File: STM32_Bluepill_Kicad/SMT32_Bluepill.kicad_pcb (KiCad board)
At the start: 2 copper layers, 2 parts, among them IC1 RT9193-33GB, U1 STM32F103C8Tx

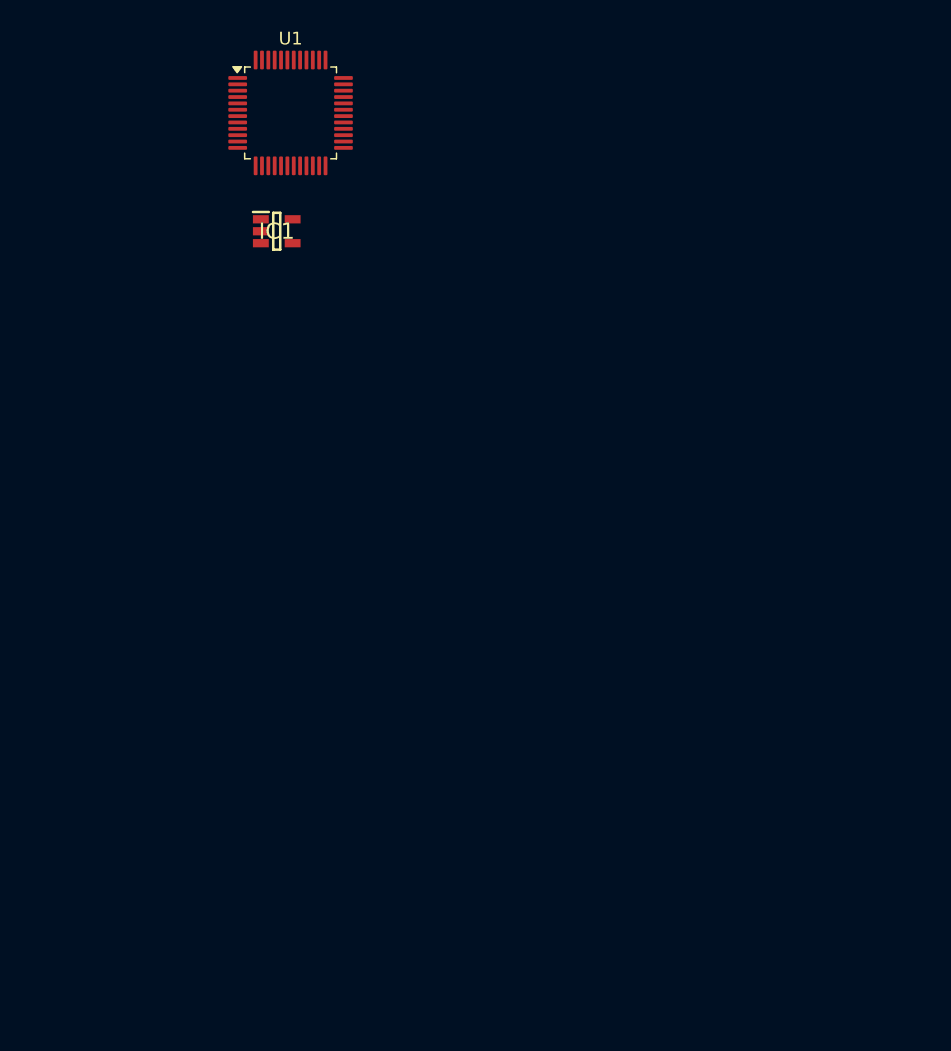
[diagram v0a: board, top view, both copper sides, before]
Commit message: Schematic done, PCB 50%
Component placements still undone
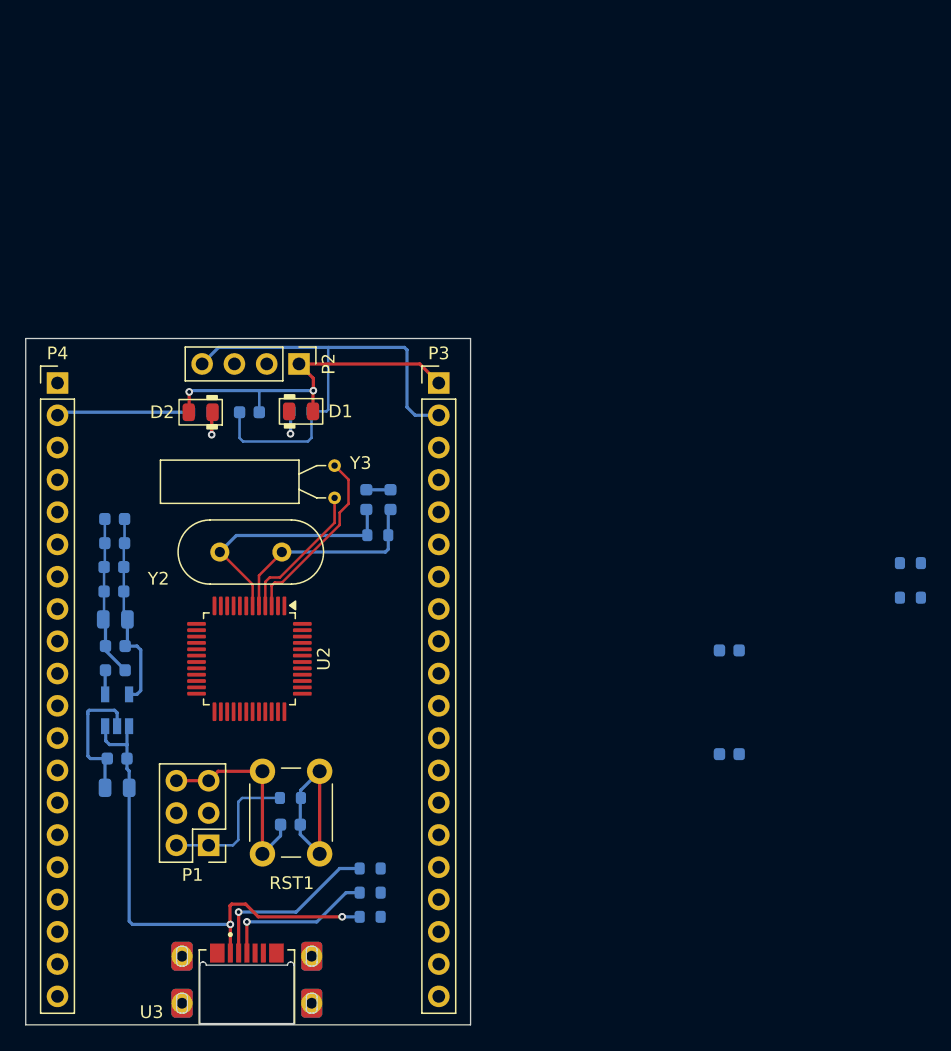
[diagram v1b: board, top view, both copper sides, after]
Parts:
- added C1: 104_0603, PCM_Capacitor_SMD_AKL:C_0603_1608Metric, B.Cu at (35.1, 52.3)
- added C10: 104_0603, PCM_Capacitor_SMD_AKL:C_0603_1608Metric, B.Cu at (24.4, 64.5)
- added C11: 104_0603, PCM_Capacitor_SMD_AKL:C_0603_1608Metric, B.Cu at (24.4, 66.4)
- added C12: 20pF_0603, PCM_Capacitor_SMD_AKL:C_0603_1608Metric, B.Cu at (72.9, 79.2)
- added C13: 20pF_0603, PCM_Capacitor_SMD_AKL:C_0603_1608Metric, B.Cu at (46.2, 59.2)
- added C14: 20pF_0603, PCM_Capacitor_SMD_AKL:C_0603_1608Metric, B.Cu at (44.3, 59.2)
- added C15: 223_0603, PCM_Capacitor_SMD_AKL:C_0603_1608Metric, B.Cu at (24.6, 72.6)
- added C2: 105_0603, PCM_Capacitor_SMD_AKL:C_0603_1608Metric, B.Cu at (38.3, 84.8)
- added C3: 104_0603, PCM_Capacitor_SMD_AKL:C_0603_1608Metric, B.Cu at (24.5, 60.7)
- added C4: 104_0603, PCM_Capacitor_SMD_AKL:C_0603_1608Metric, B.Cu at (24.5, 62.6)
- added C5: 105_0805, PCM_Capacitor_SMD_AKL:C_0805_2012Metric, B.Cu at (24.7, 81.8)
- added C6: 106_0805, PCM_Capacitor_SMD_AKL:C_0805_2012Metric, B.Cu at (24.6, 68.6)
- added C7: 104_0603, PCM_Capacitor_SMD_AKL:C_0603_1608Metric, B.Cu at (24.7, 79.5)
- added C8: 104_0603, PCM_Capacitor_SMD_AKL:C_0603_1608Metric, B.Cu at (24.6, 70.7)
- added C9: 20pF_0603, PCM_Capacitor_SMD_AKL:C_0603_1608Metric, B.Cu at (72.9, 71.0)
- added D1: LED_0805_Red, PCM_LED_SMD_AKL:LED_0805_2012Metric, F.Cu at (39.2, 52.2)
- added D2: LED_0805_Blue, PCM_LED_SMD_AKL:LED_0805_2012Metric, F.Cu at (31.3, 52.3)
- added P1: PINHD_2x3_Male, Connector_PinHeader_2.54mm:PinHeader_2x03_P2.54mm_Vertical, F.Cu at (31.9, 86.4)
- added P2: PINHD_1x4_Male, Connector_PinHeader_2.54mm:PinHeader_1x04_P2.54mm_Vertical, F.Cu at (39.0, 48.5)
- added P3: PINHD_1x20_Male, Connector_PinHeader_2.54mm:PinHeader_1x20_P2.54mm_Vertical, F.Cu at (50.0, 50.0)
- added P4: PINHD_1x20_Male, Connector_PinHeader_2.54mm:PinHeader_1x20_P2.54mm_Vertical, F.Cu at (20.0, 50.0)
- added R1: 510_0603, PCM_Resistor_SMD_AKL:R_0603_1608Metric, B.Cu at (39.2, 52.2)
- added R10: 4K7_0603, PCM_Resistor_SMD_AKL:R_0603_1608Metric, B.Cu at (44.6, 92.0)
- added R11: 20_0603, PCM_Resistor_SMD_AKL:R_0603_1608Metric, B.Cu at (44.6, 90.1)
- added R2: 10K_0603, PCM_Resistor_SMD_AKL:R_0603_1608Metric, B.Cu at (38.3, 82.7)
- added R3: 100K_0603, PCM_Resistor_SMD_AKL:R_0603_1608Metric, B.Cu at (87.1, 64.2)
- added R4: 100K_0603, PCM_Resistor_SMD_AKL:R_0603_1608Metric, B.Cu at (87.1, 66.9)
- added R5: 510_0603, PCM_Resistor_SMD_AKL:R_0603_1608Metric, B.Cu at (31.3, 52.3)
- added R6: 1M_0603, PCM_Resistor_SMD_AKL:R_0603_1608Metric, B.Cu at (45.2, 62.0)
- added R9: 20_0603, PCM_Resistor_SMD_AKL:R_0603_1608Metric, B.Cu at (44.6, 88.2)
- added RST1: Push_Button, Button_Switch_THT:SW_PUSH_6mm, F.Cu at (36.1, 87.0)
- added U3: 10103593-0001LF, USBmicro_10103593-0001LF:AMPHENOL_10103593-0001LF, F.Cu at (34.9, 98.8)
- added Y2: Crystal_8MHz, Crystal:Crystal_HC49-4H_Vertical, F.Cu at (37.6, 63.3)
- added Y3: Crystal_32.768kHz, Crystal:Crystal_AT310_D3.0mm_L10.0mm_Horizontal, F.Cu at (41.8, 56.5)
- U1: renamed from IC1; moved to B.Cu
- moved U2 43.1 mm to (35.1, 71.7), turned to -90 degrees
- moved U1 39.7 mm to (24.7, 75.8), turned to 90 degrees
- renumbered U1 to U2
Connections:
- U1 pad 1: unconnected-(IC1-VIN-Pad1) -> +5V
- U1 pad 2: unconnected-(IC1-GND-Pad2) -> GND
- U1 pad 3: unconnected-(IC1-EN-Pad3) -> +5V
- U1 pad 4: unconnected-(IC1-BP-Pad4) -> Net-(U1-BP)
- U1 pad 5: unconnected-(IC1-VOUT-Pad5) -> +3V3
- U2 pad 1: unconnected-(U1-VBAT-Pad1) -> VBAT
- U2 pad 10: unconnected-(U1-PA0-Pad10) -> PA0
- U2 pad 11: unconnected-(U1-PA1-Pad11) -> PA1
- U2 pad 12: unconnected-(U1-PA2-Pad12) -> PA2
- U2 pad 13: unconnected-(U1-PA3-Pad13) -> PA3
- U2 pad 14: unconnected-(U1-PA4-Pad14) -> PA4
- U2 pad 15: unconnected-(U1-PA5-Pad15) -> PA5
- U2 pad 16: unconnected-(U1-PA6-Pad16) -> PA6
- U2 pad 17: unconnected-(U1-PA7-Pad17) -> PA7
- U2 pad 18: unconnected-(U1-PB0-Pad18) -> PB0
- U2 pad 19: unconnected-(U1-PB1-Pad19) -> PB1
- U2 pad 2: unconnected-(U1-PC13-Pad2) -> PC13
- U2 pad 20: unconnected-(U1-PB2-Pad20) -> BOOT1
- U2 pad 21: unconnected-(U1-PB10-Pad21) -> PB10
- U2 pad 22: unconnected-(U1-PB11-Pad22) -> PB11
- U2 pad 23: Net-(U1-VSS-Pad23) -> GND
- U2 pad 24: unconnected-(U1-VDD-Pad24) -> +3V3
- U2 pad 25: unconnected-(U1-PB12-Pad25) -> PB12
- U2 pad 26: unconnected-(U1-PB13-Pad26) -> PB13
- U2 pad 27: unconnected-(U1-PB14-Pad27) -> PB14
- U2 pad 28: unconnected-(U1-PB15-Pad28) -> PB15
- U2 pad 29: unconnected-(U1-PA8-Pad29) -> PA8
- U2 pad 3: unconnected-(U1-PC14-Pad3) -> PC14
- U2 pad 30: unconnected-(U1-PA9-Pad30) -> PA9
- U2 pad 31: unconnected-(U1-PA10-Pad31) -> PA10
- U2 pad 32: unconnected-(U1-PA11-Pad32) -> PA11
- U2 pad 33: unconnected-(U1-PA12-Pad33) -> PA12
- U2 pad 34: unconnected-(U1-PA13-Pad34) -> SWDIO
- U2 pad 35: Net-(U1-VSS-Pad23) -> GND
- U2 pad 36: unconnected-(U1-VDD-Pad36) -> +3V3
- U2 pad 37: unconnected-(U1-PA14-Pad37) -> SWDCLK
- U2 pad 38: unconnected-(U1-PA15-Pad38) -> PA15
- U2 pad 39: unconnected-(U1-PB3-Pad39) -> PB3
- U2 pad 4: unconnected-(U1-PC15-Pad4) -> PC15
- U2 pad 40: unconnected-(U1-PB4-Pad40) -> PB4
- U2 pad 41: unconnected-(U1-PB5-Pad41) -> PB5
- U2 pad 42: unconnected-(U1-PB6-Pad42) -> PB6
- U2 pad 43: unconnected-(U1-PB7-Pad43) -> PB7
- U2 pad 44: unconnected-(U1-BOOT0-Pad44) -> BOOT0
- U2 pad 45: unconnected-(U1-PB8-Pad45) -> PB8
- U2 pad 46: unconnected-(U1-PB9-Pad46) -> PB9
- U2 pad 47: Net-(U1-VSS-Pad23) -> GND
- U2 pad 48: unconnected-(U1-VDD-Pad48) -> +3V3
- U2 pad 5: unconnected-(U1-PD0-Pad5) -> OSCIN
- U2 pad 6: unconnected-(U1-PD1-Pad6) -> OSCOUT
- U2 pad 7: unconnected-(U1-NRST-Pad7) -> NRST
- U2 pad 8: unconnected-(U1-VSSA-Pad8) -> GND
- U2 pad 9: unconnected-(U1-VDDA-Pad9) -> +3V3
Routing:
- net GND: track 0.00 -> 81.5 mm
- net +3V3: track 0.00 -> 56.5 mm, vias 0 -> 2
- net +5V: track 0.00 -> 40.9 mm, vias 0 -> 2
- net OSCOUT: track 0.00 -> 19.5 mm
- net OSCIN: track 0.00 -> 17.1 mm
- net PC14: track 0.00 -> 14.3 mm
- net Net-(C2-Pad1): track 0.00 -> 14.3 mm
- net Net-(U3-D-): track 0.00 -> 14.2 mm, vias 0 -> 1
- net Net-(U3-D+): track 0.00 -> 12.3 mm, vias 0 -> 1
- net PC15: track 0.00 -> 11.2 mm
- net PC13: track 0.00 -> 10.6 mm
- net Net-(D2-K): track 0.00 -> 3.58 mm, vias 0 -> 1
- net Net-(U1-BP): track 0.00 -> 1.95 mm
- net Net-(C13-Pad1): track 0.00 -> 1.90 mm
- net Net-(D1-K): track 0.00 -> 1.77 mm, vias 0 -> 1
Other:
- board outline added: 35 x 54 mm

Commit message: PCB 70%
This version haven't been to redesign
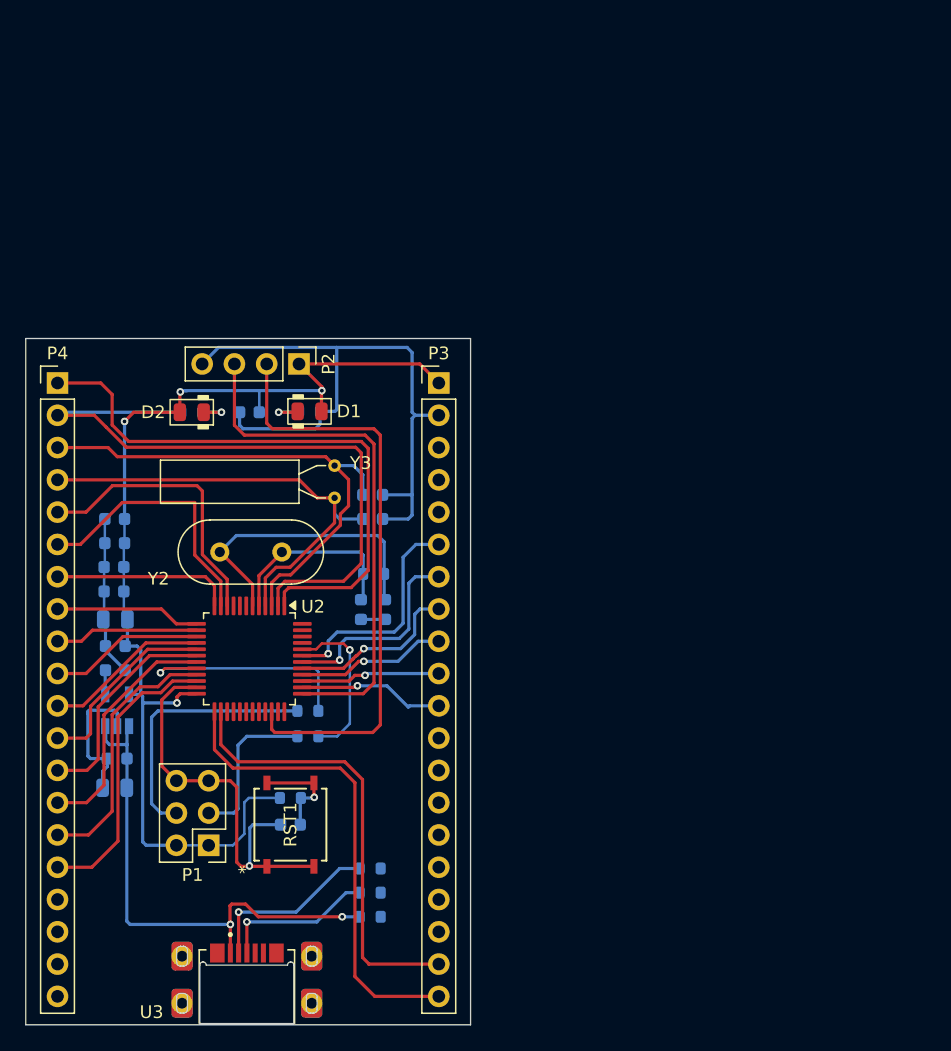
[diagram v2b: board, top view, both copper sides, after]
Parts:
- RST1: value Push_Button -> PTS526 SM15 SMTR2 LFS; footprint Button_Switch_THT:SW_PUSH_6mm -> SWST_PTS526_SM15_SMTR2_LFS:SON4_PTS526 SM15 SMTR2 LFS_CNK-M
- moved R3 49.3 mm to (39.7, 77.8)
- moved R4 48.2 mm to (39.7, 75.8), turned to 0 degrees
- moved C12 33.6 mm to (44.8, 60.7)
- moved C9 30.6 mm to (44.8, 58.8)
- moved C13 8.96 mm to (43.9, 67.8), turned to 90 degrees
- moved C14 8.77 mm to (45.8, 67.8), turned to 90 degrees
- moved RST1 3.18 mm to (38.3, 84.8)
- moved R6 3.07 mm to (44.9, 65.0), turned to 180 degrees
- moved D2 0.70 mm to (30.6, 52.3)
- moved R5 0.70 mm to (30.6, 52.3)
- moved D1 0.67 mm to (39.8, 52.2)
- moved R1 0.67 mm to (39.8, 52.2)
- moved C5 0.19 mm to (24.5, 81.8)
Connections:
- RST1 pad 2: Net-(C2-Pad1) -> GND
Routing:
- net SWDIO: track 0.00 -> 47.1 mm
- net VBAT: track 0.00 -> 46.1 mm
- net PC13: track 10.6 -> 52.5 mm
- net SWDCLK: track 0.00 -> 41.2 mm
- net PB12: track 0.00 -> 37.6 mm
- net PB13: track 0.00 -> 35.1 mm
- net +3V3: track 56.5 -> 90.3 mm, vias 2 -> 4
- net GND: track 81.5 -> 108.6 mm, vias 0 -> 1
- net PC14: track 14.3 -> 41.0 mm
- net PC15: track 11.2 -> 37.5 mm
- net PB11: track 0.00 -> 22.7 mm
- net PA0: track 0.00 -> 22.3 mm
- net PA1: track 0.00 -> 21.2 mm
- net Net-(P1-Pad4): track 0.00 -> 20.7 mm
- net PB10: track 0.00 -> 20.6 mm
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
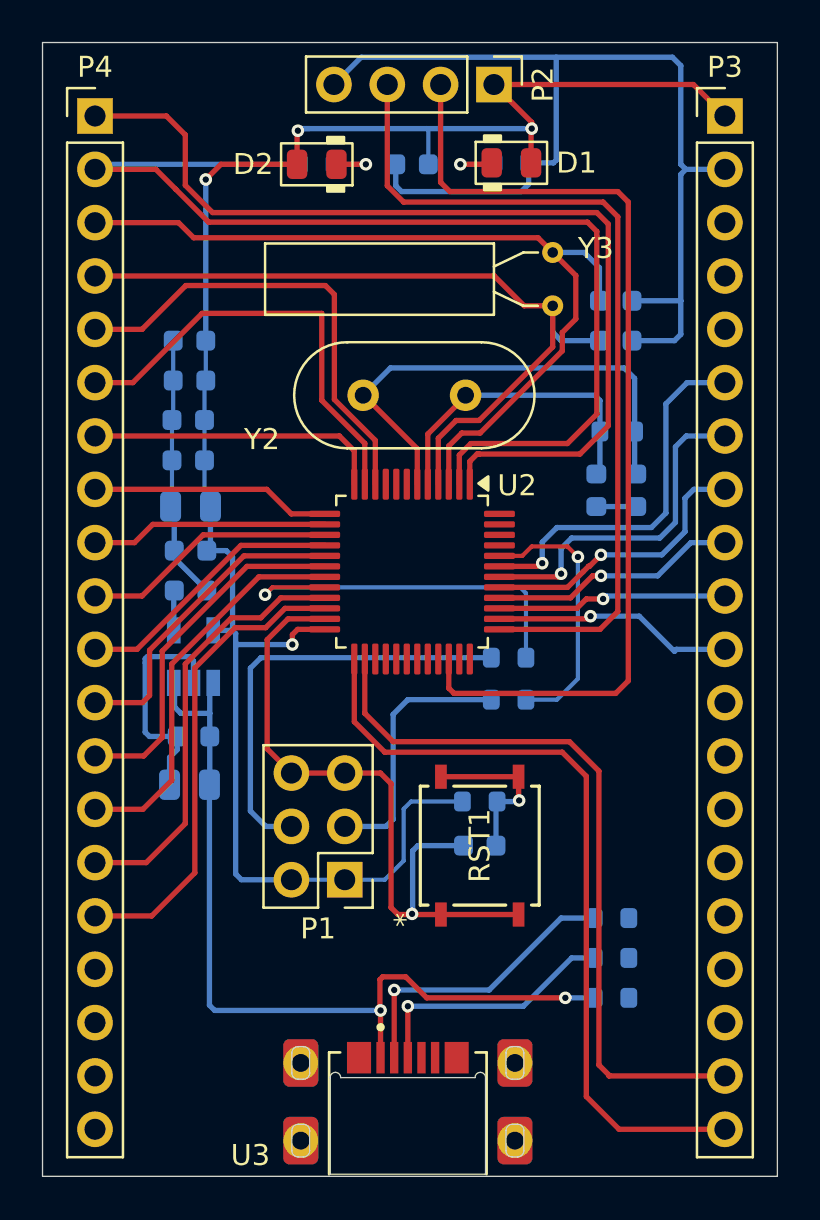
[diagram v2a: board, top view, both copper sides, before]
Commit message: PCB 80%
There are some traces that need to be retraced
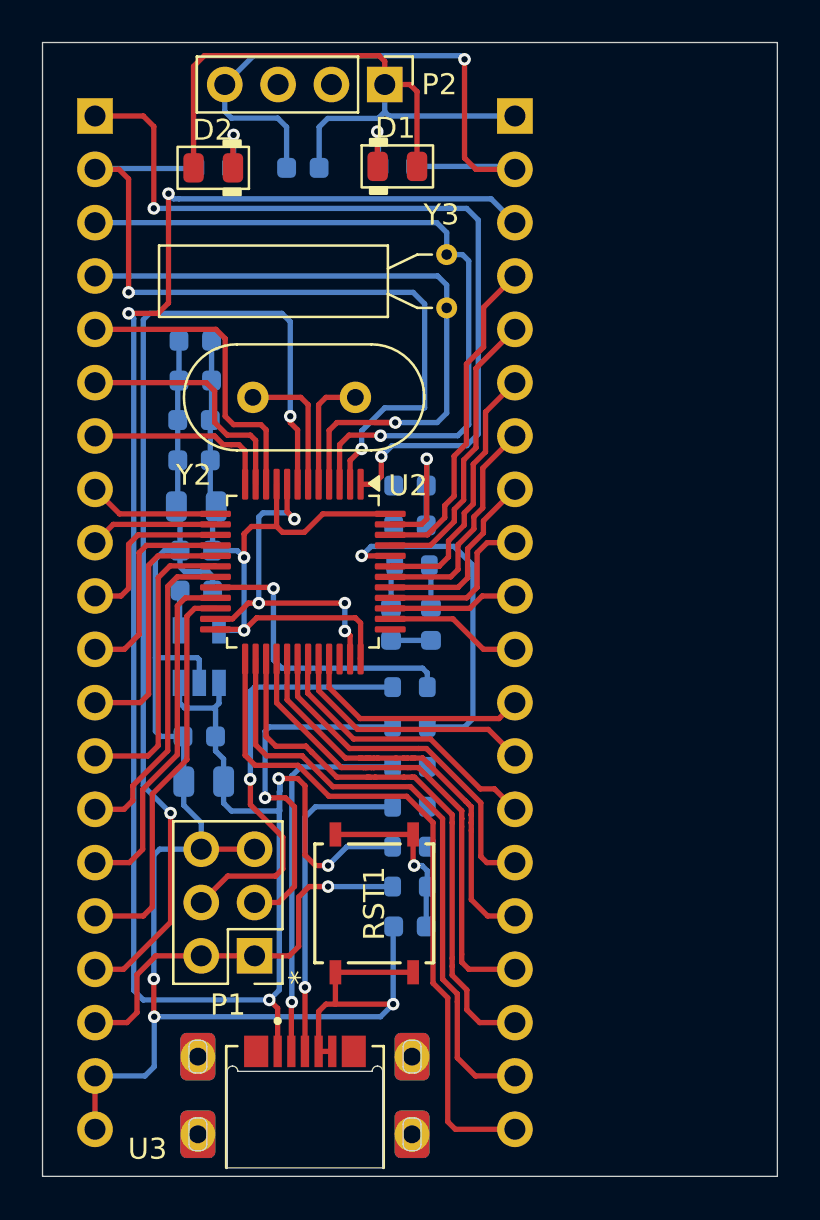
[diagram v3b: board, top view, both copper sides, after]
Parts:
- P3, P4: moved to B.Cu
- moved C12 13.2 mm to (35.0, 69.5)
- moved C9 13.2 mm to (35.0, 67.6)
- moved R10 12.0 mm to (35.0, 84.8)
- moved R9 12.0 mm to (35.0, 81.0)
- moved R11 12.0 mm to (35.0, 82.9)
- moved C13 11.7 mm to (34.1, 74.2)
- moved C14 11.7 mm to (36.0, 74.2)
- moved R6 11.7 mm to (35.1, 71.4)
- moved P3 10.0 mm to (40.0, 50.0), turned to 180 degrees
- moved RST1 5.73 mm to (33.3, 87.5)
- moved P1 5.62 mm to (27.6, 90.0)
- moved D1 5.43 mm to (34.4, 52.4)
- moved R1 5.43 mm to (34.4, 52.4)
- moved Y2 5.25 mm to (32.4, 63.4)
- moved R2 5.24 mm to (35.0, 86.7)
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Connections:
- P4 pad 18: 3V3 -> +3V3
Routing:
- net +5V: track 41.0 -> 99.3 mm, vias 2 -> 5
- net NRST: track 0.00 -> 48.9 mm, vias 0 -> 2
- net SWDIO: track 47.1 -> 0.00 mm
- net SWDCLK: track 41.2 -> 0.00 mm
- net GND: track 108.6 -> 136.3 mm, vias 1 -> 9
- net PB14: track 0.00 -> 26.2 mm
- net PB15: track 0.00 -> 22.9 mm
- net PA8: track 0.00 -> 19.6 mm
- net PA9: track 0.00 -> 16.9 mm
- net PB9: track 0.00 -> 15.8 mm
- net PC13: track 52.5 -> 37.5 mm, vias 0 -> 2
- net OSCOUT: track 23.3 -> 8.62 mm
- net PB8: track 0.00 -> 13.9 mm
- net PA10: track 0.00 -> 13.8 mm
- net PA11: track 0.00 -> 12.1 mm
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
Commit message: Final R0
Done R0
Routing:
- net +3V3: track 89.1 -> 151.7 mm, vias 3 -> 4
- net SWDCLK: track 0.00 -> 53.1 mm
- net SWDIO: track 0.00 -> 50.1 mm, vias 0 -> 2
- net GND: track 136.3 -> 181.6 mm, vias 9 -> 11
- net PA12: track 11.1 -> 24.0 mm
- net OSCIN: track 7.78 -> 17.8 mm, vias 0 -> 1
- net OSCOUT: track 8.62 -> 17.8 mm, vias 0 -> 1
- net PA11: track 12.1 -> 16.5 mm
- net PC15: track 32.5 -> 36.1 mm, vias 1 -> 2
- net PC14: track 35.4 -> 38.6 mm, vias 1 -> 2
- net BOOT0: track 16.9 -> 14.4 mm
- net NRST: track 48.9 -> 49.9 mm
- added copper zone on B.Cu, net GND
- added copper zone on F.Cu, net GND
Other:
- board size 35 x 54 mm -> 25 x 54 mm
